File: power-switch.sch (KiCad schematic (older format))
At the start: 11 parts, among them U2 TPS1HB08A-Q1

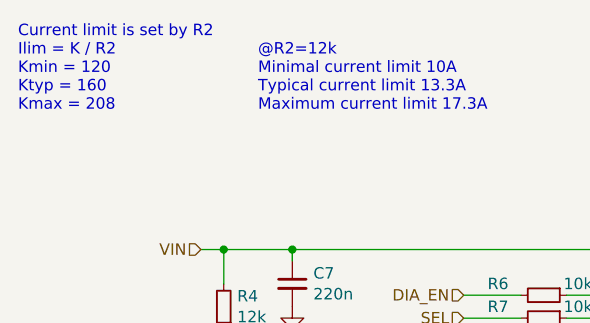
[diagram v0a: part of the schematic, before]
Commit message: Add fiducials, fix aesthetics in schematics
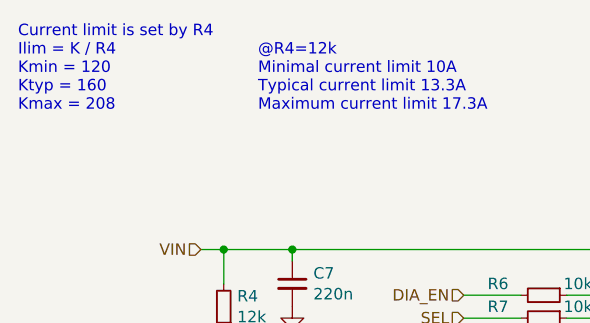
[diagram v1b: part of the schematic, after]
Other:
- note added: "@R4=12k\nMinimal current limit 10A\nTypical current limit 13.3A\nMaximum current limit 17.3A"
- note added: "Current limit is set by R4\nIlim = K / R4\nKmin = 120\nKtyp = 160\nKmax = 208"
- note removed: "@R2=12k\nMinimal current limit 10A\nTypical current limit 13.3A\nMaximum current limit 17.3A"
- note removed: "Current limit is set by R2\nIlim = K / R2\nKmin = 120\nKtyp = 160\nKmax = 208"
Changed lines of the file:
@@
 encoding utf-8
 Sheet 6 6
-Title ""
+Title "Tougher INA3221 Power Meter"
 Date ""
 Rev ""
-Comp ""
+Comp "Beast Devices"
 Comment1 ""
 Comment2 ""
@@
 Connection ~ 7400 3050
 Text Notes 3300 2450 0    50   ~ 0
-Current limit is set by R2\nIlim = K / R2\nKmin = 120\nKtyp = 160\nKmax = 208
+Current limit is set by R4\nIlim = K / R4\nKmin = 120\nKtyp = 160\nKmax = 208
 Text Notes 4350 2450 0    50   ~ 0
-@R2=12k\nMinimal current limit 10A\nTypical current limit 13.3A\nMaximum current limit 17.3A
+@R4=12k\nMinimal current limit 10A\nTypical current limit 13.3A\nMaximum current limit 17.3A
 Text HLabel 8200 3050 2    50   Output ~ 0
 VOUT

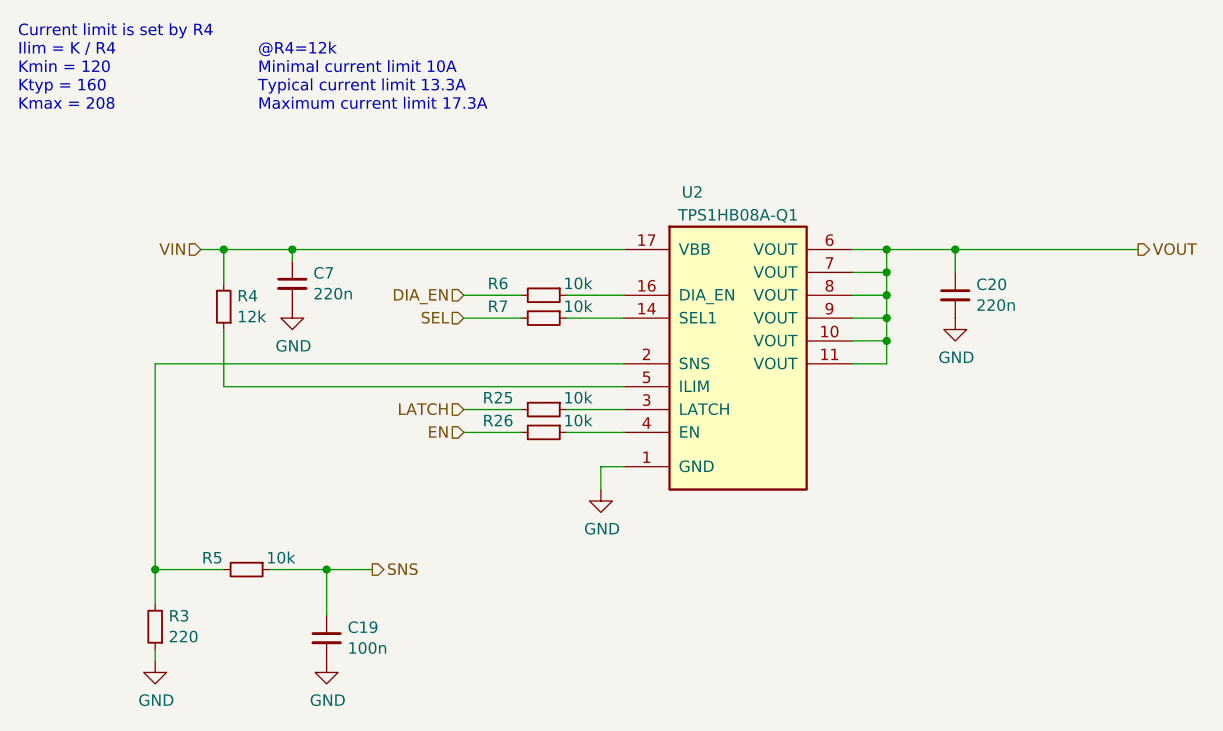
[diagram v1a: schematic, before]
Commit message: Add manufacturers, part numbers, and supplier links
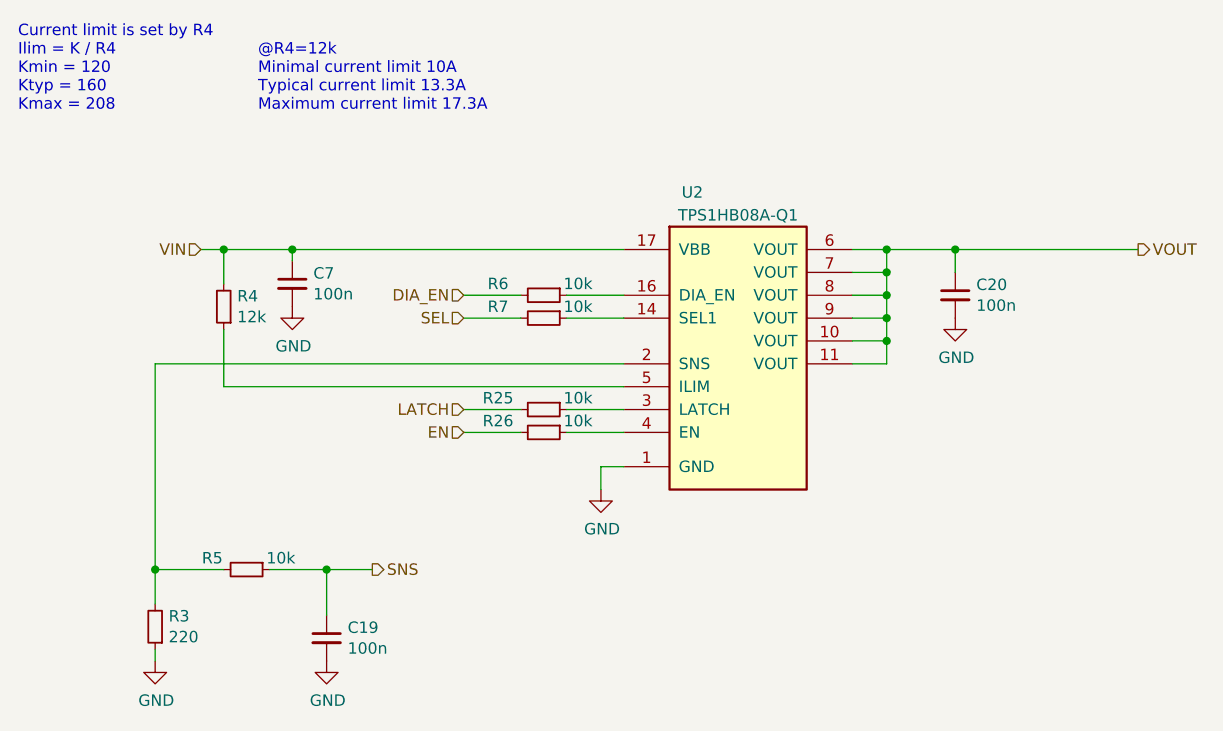
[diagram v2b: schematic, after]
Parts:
- C19: footprint Resistor_SMD:R_0603_1608Metric -> Capacitor_SMD:C_0603_1608Metric; Voltage (none) -> 50V
- C20, C7: value 220n -> 100n; Voltage (none) -> 50V
- R25, R26, R3, R4, R5, R6, R7: Tolerance (none) -> 1%
- U2: Distributor Link (none) -> https://www.digikey.se/product-detail/en/texas-instruments/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; Manufacturer (none) -> Texas Instruments; Part Number (none) -> TPS1HB08AQPWPRQ1
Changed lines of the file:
@@
 F 2 "Package_SO:HTSSOP-16-1EP_4.4x5mm_P0.65mm_EP3.4x5mm" H 6450 3750 50  0001 C CNN
 F 3 "http://www.ti.com/lit/ds/symlink/tps2042.pdf" H 6400 3550 50  0001 C CNN
+F 4 "https://www.digikey.se/product-detail/en/texas-instruments/TPS1HB08AQPWPRQ1/296-TPS1HB08AQPWPRQ1CT-ND/11615930" H 6450 3250 50  0001 C CNN "Distributor Link"
+F 5 "Texas Instruments" H 6450 3250 50  0001 C CNN "Manufacturer"
+F 6 "TPS1HB08AQPWPRQ1" H 6450 3250 50  0001 C CNN "Part Number"
 	1    6450 3250
 	1    0    0    -1
@@
 F 2 "Resistor_SMD:R_0603_1608Metric" H 3900 4700 50  0001 C CNN
 F 3 "~" H 3900 4700 50  0001 C CNN
+F 4 "1%" H 3900 4700 50  0001 C CNN "Tolerance"
 	1    3900 4700
 	-1   0    0    1
@@
 F 2 "Resistor_SMD:R_0603_1608Metric" H 4200 3300 50  0001 C CNN
 F 3 "~" H 4200 3300 50  0001 C CNN
+F 4 "1%" H 4200 3300 50  0001 C CNN "Tolerance"
 	1    4200 3300
 	-1   0    0    1
@@
 F 2 "Resistor_SMD:R_0603_1608Metric" H 5600 3750 50  0001 C CNN
 F 3 "~" H 5600 3750 50  0001 C CNN
+F 4 "1%" H 5600 3750 50  0001 C CNN "Tolerance"
 	1    5600 3750
 	0    1    1    0
@@
 F 2 "Resistor_SMD:R_0603_1608Metric" H 5600 3850 50  0001 C CNN
 F 3 "~" H 5600 3850 50  0001 C CNN
+F 4 "1%" H 5600 3850 50  0001 C CNN "Tolerance"
 	1    5600 3850
 	0    1    1    0
@@
 F 2 "Resistor_SMD:R_0603_1608Metric" H 5600 3350 50  0001 C CNN
 F 3 "~" H 5600 3350 50  0001 C CNN
+F 4 "1%" H 5600 3350 50  0001 C CNN "Tolerance"
 	1    5600 3350
 	0    1    1    0
@@
 F 2 "Resistor_SMD:R_0603_1608Metric" H 5600 3250 50  0001 C CNN
 F 3 "~" H 5600 3250 50  0001 C CNN
+F 4 "1%" H 5600 3250 50  0001 C CNN "Tolerance"
 	1    5600 3250
 	0    1    1    0
@@
 AR Path="/5F64E916/5F65AA22" Ref="C20"  Part="1"
 F 0 "C20" H 7492 3296 50  0000 L CNN
-F 1 "220n" H 7492 3205 50  0000 L CNN
+F 1 "100n" H 7492 3205 50  0000 L CNN
 F 2 "Capacitor_SMD:C_0603_1608Metric" H 7400 3250 50  0001 C CNN
 F 3 "~" H 7400 3250 50  0001 C CNN
+F 4 "50V" H 7400 3250 50  0001 C CNN "Voltage"
 	1    7400 3250
 	1    0    0    -1
@@
 AR Path="/5F64E916/5F65AA28" Ref="C7"  Part="1"
 F 0 "C7" H 4592 3246 50  0000 L CNN
-F 1 "220n" H 4592 3155 50  0000 L CNN
+F 1 "100n" H 4592 3155 50  0000 L CNN
 F 2 "Capacitor_SMD:C_0603_1608Metric" H 4500 3200 50  0001 C CNN
 F 3 "~" H 4500 3200 50  0001 C CNN
+F 4 "50V" H 4500 3200 50  0001 C CNN "Voltage"
 	1    4500 3200
 	1    0    0    -1
@@
 F 2 "Resistor_SMD:R_0603_1608Metric" H 4300 4450 50  0001 C CNN
 F 3 "~" H 4300 4450 50  0001 C CNN
+F 4 "1%" H 4300 4450 50  0001 C CNN "Tolerance"
 	1    4300 4450
 	0    1    1    0
@@
 F 0 "C19" H 4742 4796 50  0000 L CNN
 F 1 "100n" H 4742 4705 50  0000 L CNN
-F 2 "Resistor_SMD:R_0603_1608Metric" H 4650 4750 50  0001 C CNN
+F 2 "Capacitor_SMD:C_0603_1608Metric" H 4650 4750 50  0001 C CNN
 F 3 "~" H 4650 4750 50  0001 C CNN
+F 4 "50V" H 4650 4750 50  0001 C CNN "Voltage"
 	1    4650 4750
 	1    0    0    -1
